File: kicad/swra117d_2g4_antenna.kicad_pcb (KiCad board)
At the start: 2 copper layers, 40 x 30 mm, 5 parts, among them J1 SMA edge launch

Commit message: Ship the board unmatched: L1 is a 0 ohm jumper
The SWRA117D antenna is a 50 ohm design, so the board should leave the
factory with nothing matched out. L1 was defaulting to the 0.8 nH the
lumped model prefers, which put reactance in the path of an antenna that
does not need it. L1 is now a 0 ohm jumper and C1/C2 stay unpopulated, so
the RF path is connector -> 50 ohm line -> antenna and the pi network is
three empty footprints kept for retuning the assembled product.

The ngspice testbench now defaults to the as-built population (l1=1p) and
documents the 0.8 nH case as a comparison. Unmatched, the model clears
-10 dB over the whole ISM band (-10.5 dB at 2.400 GHz, -26.3 dB at
2.4835 GHz, best -29 dB at 2.493 GHz), which is the evidence that no match
is needed; 0.8 nH buys ~8 dB at band centre and moves resonance 30 MHz
down. README documents both columns and why the footprints exist at all:
stackup, ground plane size, FR4 tolerance and enclosure loading.

No change to nets, pads or routing.

Co-Authored-By: Claude Opus 5 <noreply@anthropic.com>
Claude-Session: https://claude.ai/code/session_01Prj6bUQ2KQzzxzD4bgtswJ
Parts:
- L1: value 0.8nH -> 0R
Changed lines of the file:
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@@
 			(unlocked yes)
 		)
-		(property "Value" "0.8nH"
+		(property "Value" "0R"
 			(at 0 1.16 0)
 			(layer "F.Fab")

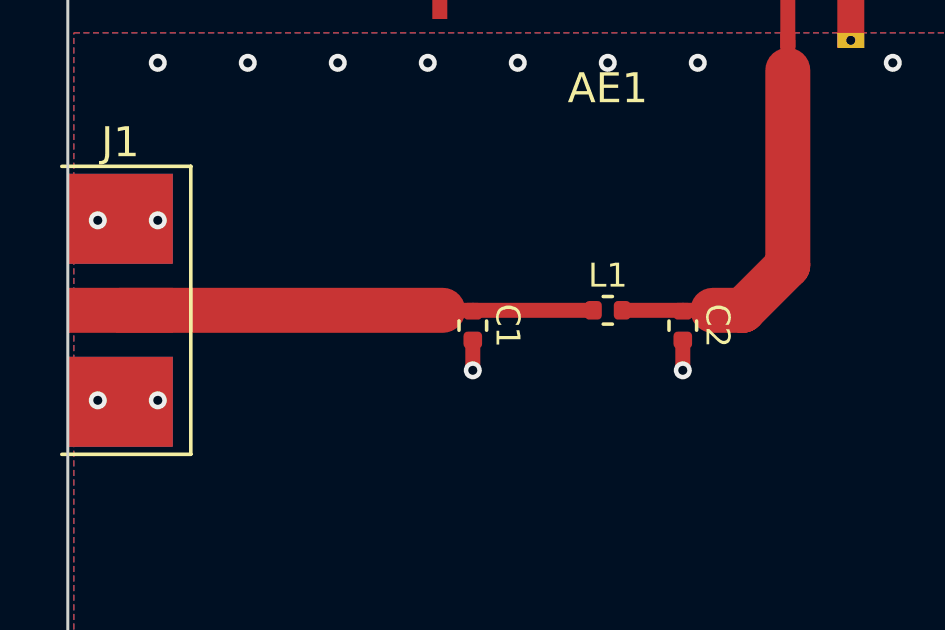
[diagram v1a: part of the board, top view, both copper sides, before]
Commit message: Feed the radiator straight from the SMA port, drop the matching network
The SWRA117D antenna is a 50 ohm design, so the board now goes connector ->
50 ohm line -> radiator with nothing in between. C1, L1 and C2 are gone
from the schematic and the board, RF_IN and ANT_FEED collapse into one net
ANT_FEED, and the feed is a single 1.5 mm microstrip run of 32.1 mm from
the SMA signal pad to the antenna feed pad: one 45 degree corner and a
1 mm neck down to 0.5 mm to meet the feed pad. A 0 ohm jumper would still
have added a few tenths of a nH and two pad discontinuities, which is the
wrong thing to have in the path when the point is to measure the antenna.

The 0402 land and the C/L symbols stay in the libraries, and the pi
topology stays in the ngspice deck as a comment, so a match can be worked
out and added if the enclosed product needs one.

Simulation now mirrors the board:
- sim/s11_pi_match.cir -> sim/s11_antenna.cir: antenna behind a lossless
  50 ohm T line (32.1 mm, TD = 195 ps), so S11 is referenced to the
  connector like a VNA measurement. -10.5 dB at 2.400 GHz, -15.4 dB at
  2.442 GHz, -26.4 dB at 2.4835 GHz, best -28.8 dB at 2.493 GHz, under
  -10 dB from 2.394 to 2.595 GHz. The line rotates Zin 172 degrees but
  cannot change |S11|, which is why the lumped model still answers the
  return-loss question.
- openEMS: the model no longer assumes a straight feed. It reads the actual
  track segments and their widths, launches the port at the board edge in
  place of the connector, and rebuilds the top pour as boxes around the
  keep-away corridors it reads from the rule areas (6 boxes, 2 corridors).

Also: the schematic now embeds only the symbols it places (4, was 6),
which is what KiCad writes itself.

Co-Authored-By: Claude Opus 5 <noreply@anthropic.com>
Claude-Session: https://claude.ai/code/session_01Prj6bUQ2KQzzxzD4bgtswJ
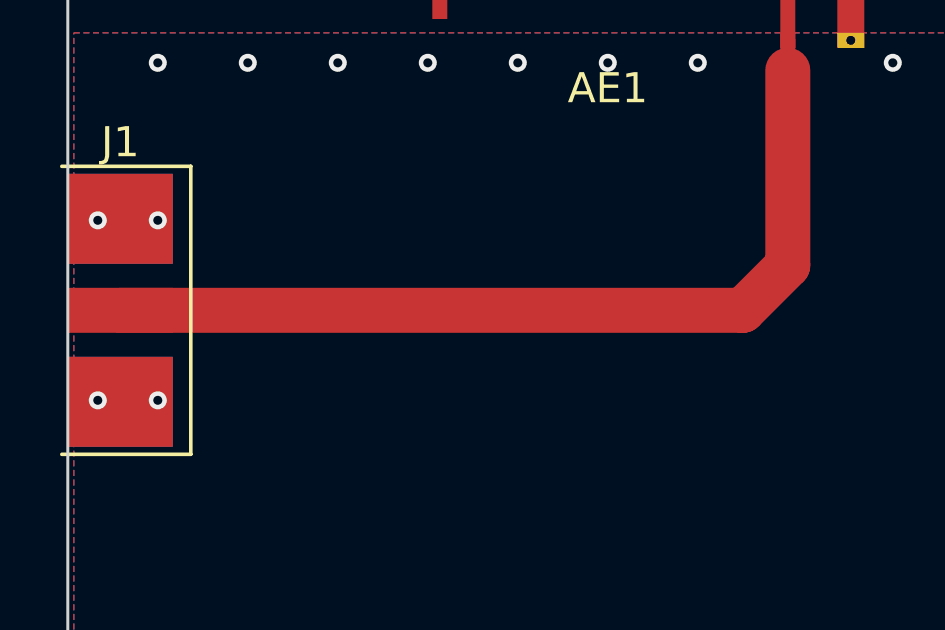
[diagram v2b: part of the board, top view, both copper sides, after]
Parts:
- removed C1, C2: 0.5pF, SWRA117D_RF:Chip_0402_1005Metric_RF
- removed L1: 0R, SWRA117D_RF:Chip_0402_1005Metric_RF
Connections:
- J1 pad 1: RF_IN -> ANT_FEED
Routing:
- net ANT_FEED: track 13.6 -> 30.4 mm
- net RF_IN: track 15.8 -> 0.00 mm
- net GND: track 2.02 -> 0.00 mm, vias 17 -> 15
